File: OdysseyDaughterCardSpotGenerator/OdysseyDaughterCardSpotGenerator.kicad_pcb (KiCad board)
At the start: 2 copper layers, 37.1 x 46.6 mm, 22 parts, among them J1 Conn_01x03, J2 Conn_01x04, Q1 2N3904, Q2 2N3904, Q3 BC547C, Q4 2N3904, X1 OdysseyDaughterCard

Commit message: OdysseyDaughterCardSpotGenerator: Open and close in KiCad 6, fix symbol library path
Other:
- net class Default removed

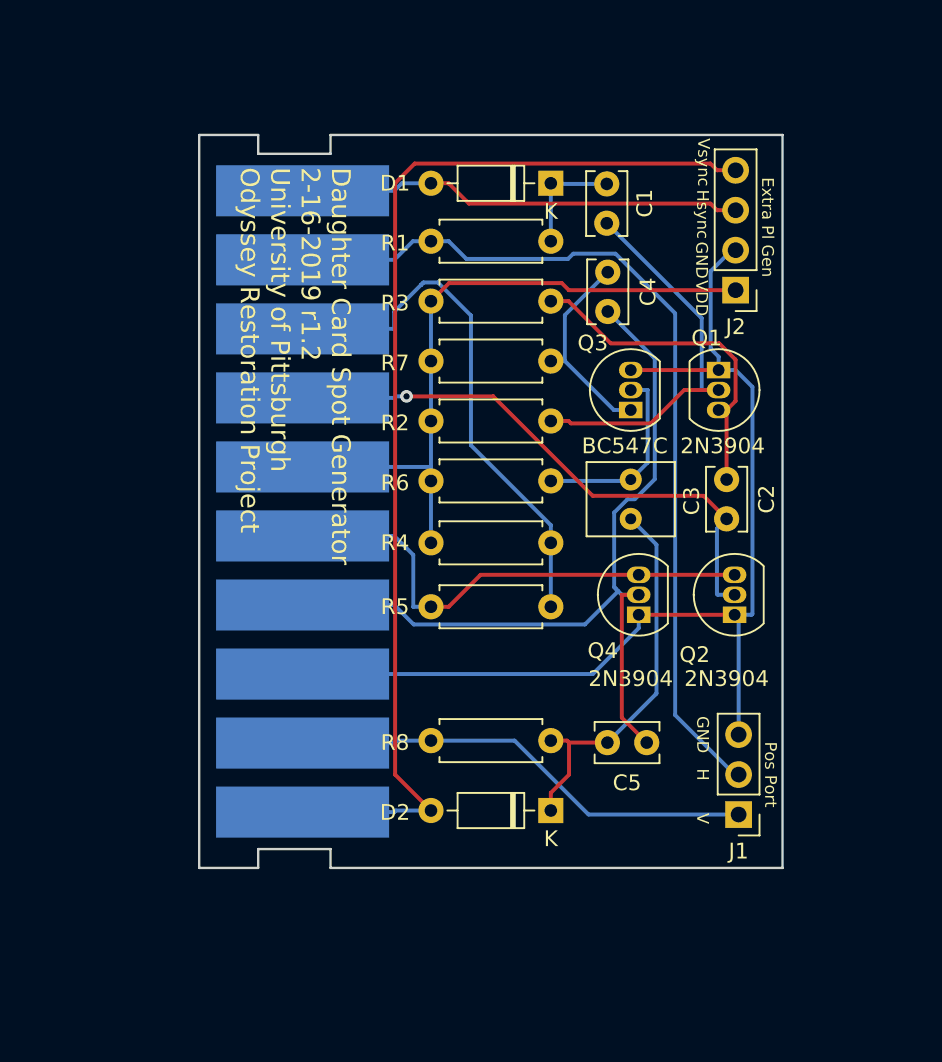
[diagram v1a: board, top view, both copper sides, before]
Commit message: OdysseyDaughterCardSpotGenerator wider transistor footprint, add logo, generate pdf, images, 3d models
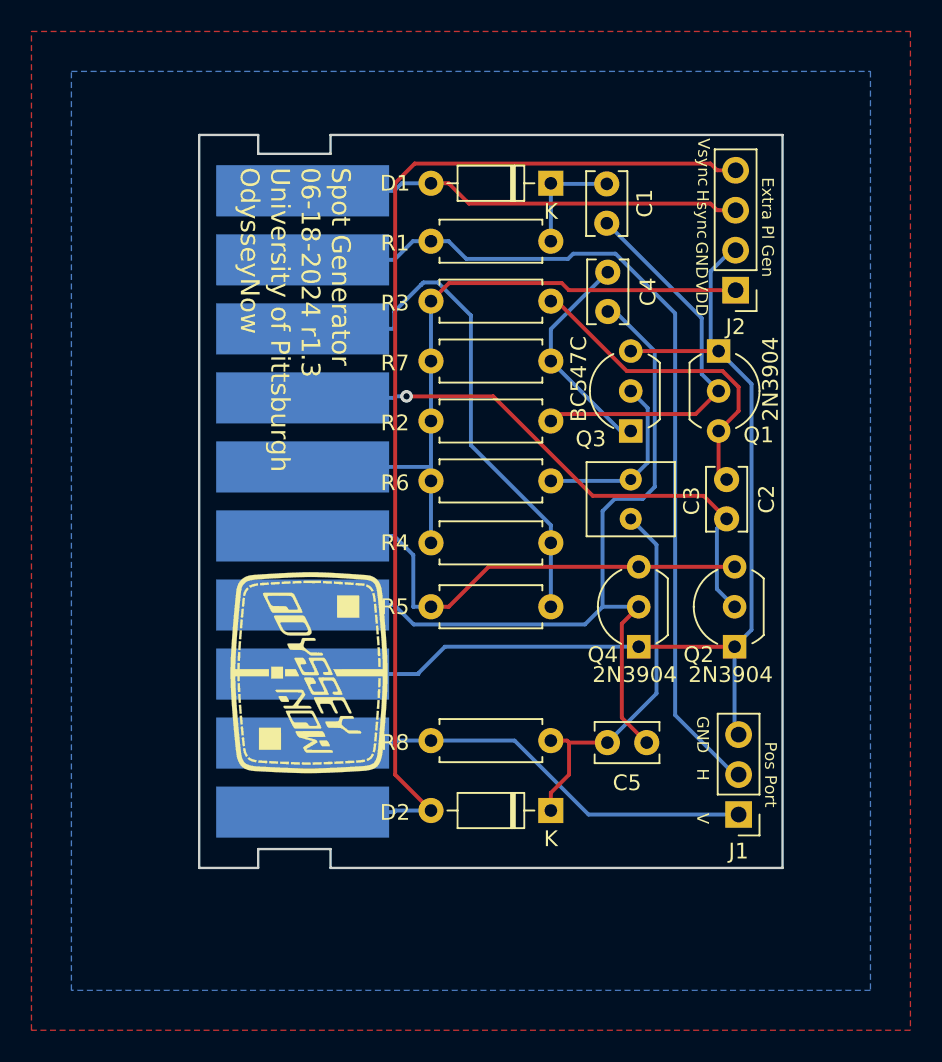
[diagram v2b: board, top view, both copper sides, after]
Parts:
- added X2: OdysseyNow_Logo, Odyssey_Daughter_Card:OdysseyNowLogo, F.Cu at (130.2, 111.6)
- Q1, Q2, Q3, Q4: footprint Package_TO_SOT_THT:TO-92_Inline -> Package_TO_SOT_THT:TO-92_Inline_Wide
- moved Q2 2.03 mm to (156.5, 110.2)
- moved Q4 2.03 mm to (150.4, 110.2)
- moved Q3 1.33 mm to (149.9, 96.5)
- moved Q1 1.21 mm to (155.4, 91.4)
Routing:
- net GND: track 69.7 -> 67.0 mm
- net Net-(Q3-C): track 13.1 -> 14.1 mm
- net Net-(Q1-C): track 21.6 -> 20.8 mm
- net Net-(Q1-B): track 25.8 -> 25.1 mm
- net Net-(Q3-B): track 12.3 -> 11.6 mm
- added copper zone on F.Cu, net /Card6
- added copper zone on B.Cu, net GND
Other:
- board text added: "Spot Generator 06-18-2024 r1.3 University of Pittsburgh OdysseyNow"
- board text removed: "Daughter Card Spot Generator 2-16-2019 r1.2 University of Pittsburgh Odyssey Restoration Project"
